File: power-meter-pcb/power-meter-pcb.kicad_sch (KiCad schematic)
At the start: 22 parts, among them J1 Crank interconnect, J2 Debug, SW1 EN, SW2 BOOT, U2 P3T1755, U8 ESP32-S3-MINI-1

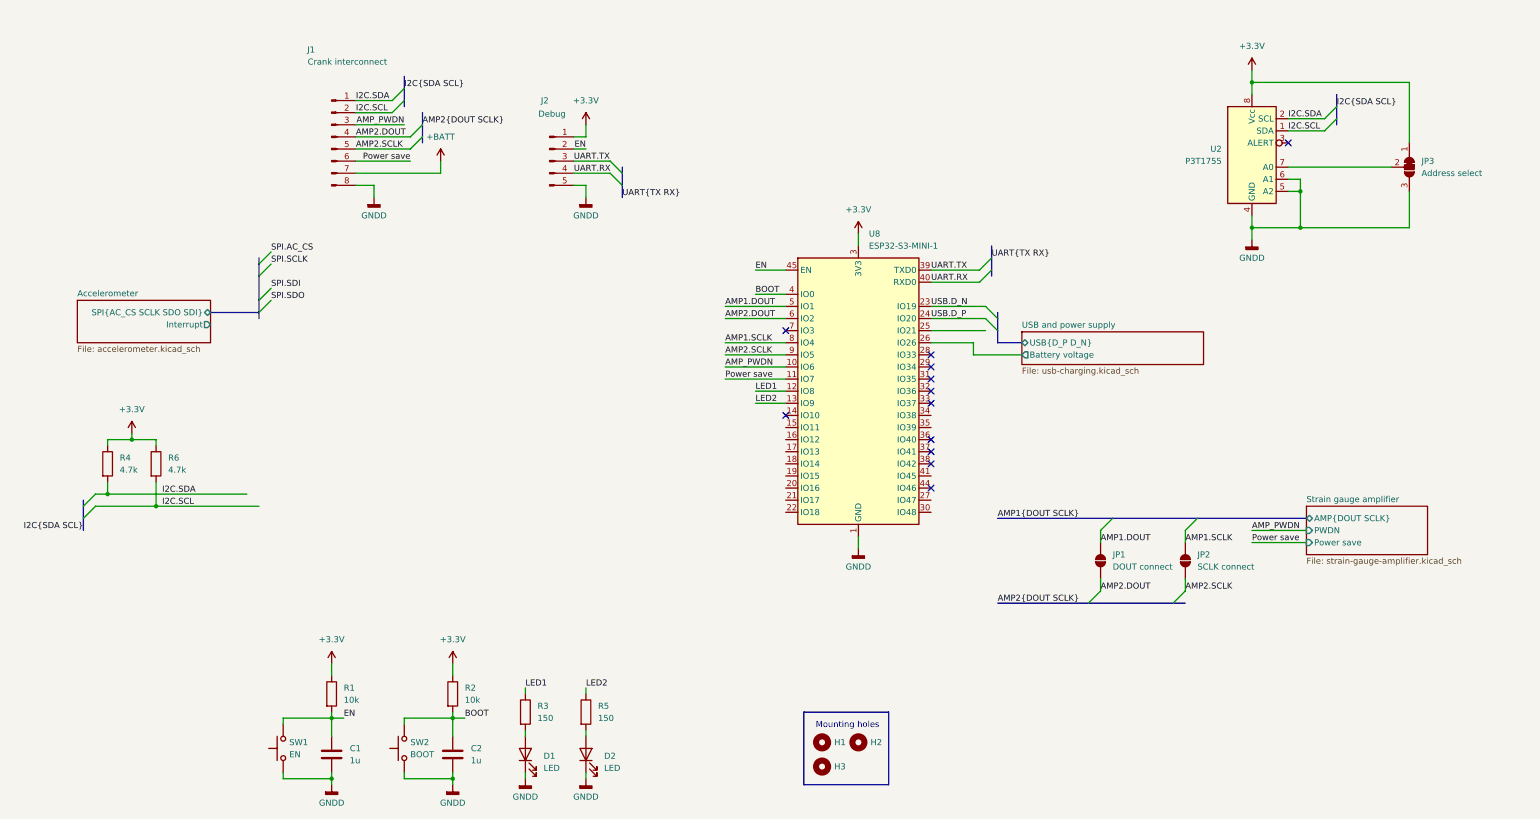
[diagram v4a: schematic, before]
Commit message: Board mostly routed, schematic page layout cleaned up
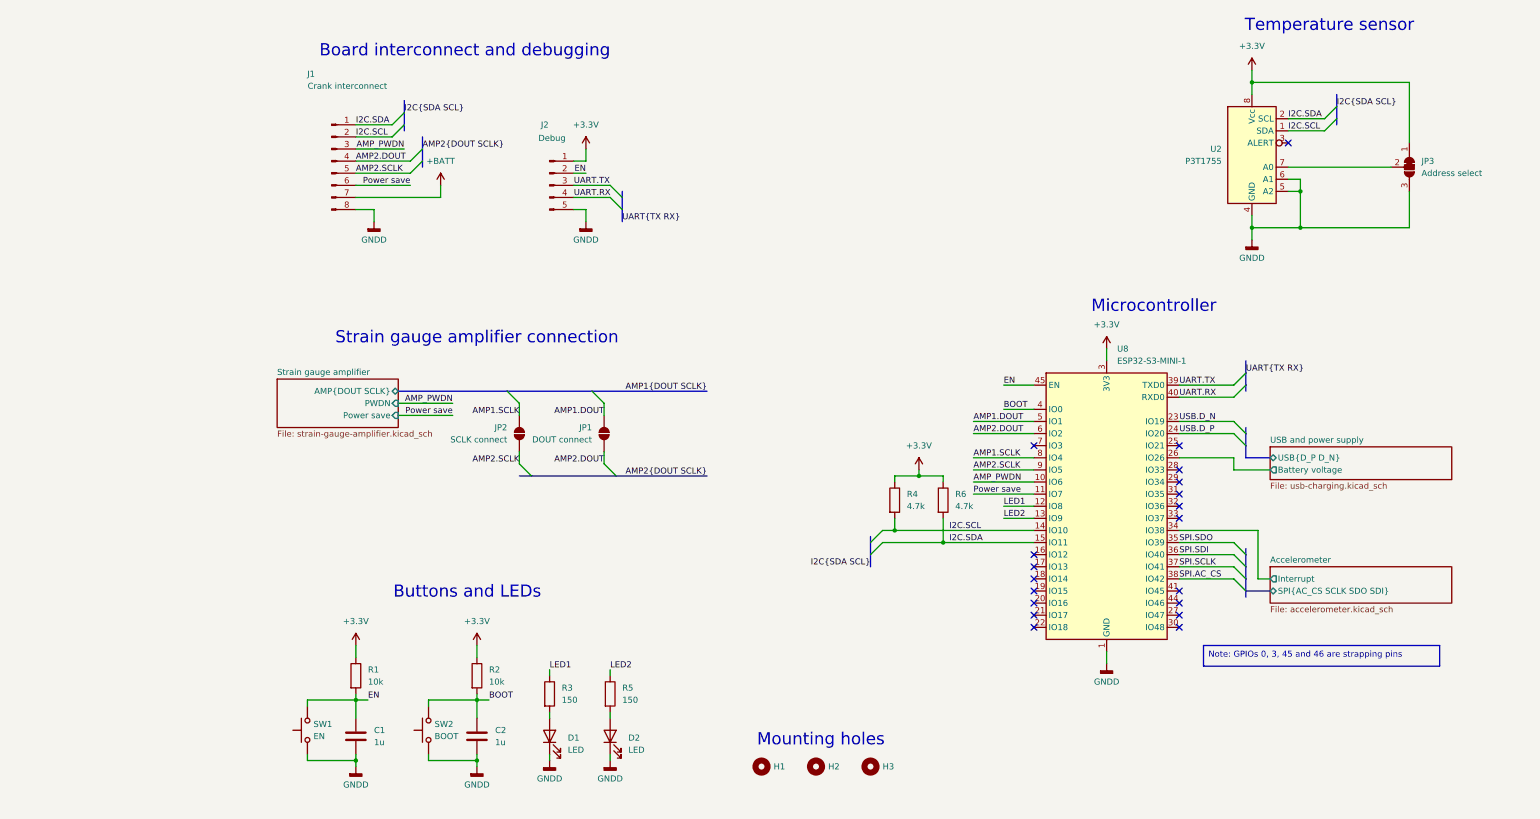
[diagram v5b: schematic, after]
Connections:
- net Accelerometer/Interrupt: now also U8.34 (IO38)
- net I2C.SCL: now also R4.2, U8.14 (IO10); no longer R6.2
- net I2C.SDA: now also R6.2, U8.15 (IO11); no longer R4.2
- net SPI.AC_CS: now also U8.38 (IO42)
- net SPI.SCLK: now also U8.37 (IO41)
- net SPI.SDI: now also U8.36 (IO40)
- net SPI.SDO: now also U8.35 (IO39)
- no-connect marks 12 -> 19
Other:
- note added: "Board interconnect and debugging"
- note added: "Buttons and LEDs"
- note added: "Microcontroller"
- note added: "Strain gauge amplifier connection"
- note added: "Temperature sensor"
- moved on the sheet: C1, C2, D1, D2, H1, H2, H3, J1, J2, JP1, JP2, R1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
